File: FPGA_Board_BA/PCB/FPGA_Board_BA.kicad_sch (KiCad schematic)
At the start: 0 parts

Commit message: started component placement
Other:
- note added: "TODO: - 25uF Kondensator -> 3 mal 10uF [X] Extra 5VA für Tamura Sensoren [X] INA Spannungspegel / Bereich Prüfen [X] SMD 2*4 pin (2.54 pitch) stecker suchen Stiftleiste [X] Wannenstecker / Buchse für FPGA free Pins (26pin) kein 5VA, zweite Reihe Für GND - ESD Protection für Tamura PinHeaders - Silkscreen bei FPGA korrigieren - Matchy 3D model für Plug Terminals"
- note removed: "TODO: - 25uF Kondensator -> 3 mal 10uF [X] Extra 5VA für Tamura Sensoren [X] INA Spannungspegel / Bereich Prüfen [X] SMD 2*4 pin (2.54 pitch) stecker suchen Stiftleiste [X] Wannenstecker / Buchse für FPGA free Pins (26pin) kein 5VA, zweite Reihe Für GND"
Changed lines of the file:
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@@
 	(generator_version "9.0")
 	(paper "A3")
-	(text "TODO:\n- 25uF Kondensator -> 3 mal 10uF \n[X] Extra 5VA für Tamura Sensoren\n[X] INA Spannungspegel / Bereich Prüfen\n[X] SMD 2*4 pin (2.54 pitch) stecker suchen Stiftleiste\n[X] Wannenstecker / Buchse für FPGA free Pins (26pin) kein 5VA, zweite Reihe\nFür GND"
+	(text "TODO:\n- 25uF Kondensator -> 3 mal 10uF \n[X] Extra 5VA für Tamura Sensoren\n[X] INA Spannungspegel / Bereich Prüfen\n[X] SMD 2*4 pin (2.54 pitch) stecker suchen Stiftleiste\n[X] Wannenstecker / Buchse für FPGA free Pins (26pin) kein 5VA, zweite Reihe\nFür GND\n- ESD Protection für Tamura PinHeaders\n- Silkscreen bei FPGA korrigieren\n- Matchy 3D model für Plug Terminals"
 		(exclude_from_sim no)
 		(at 328.422 239.268 0)

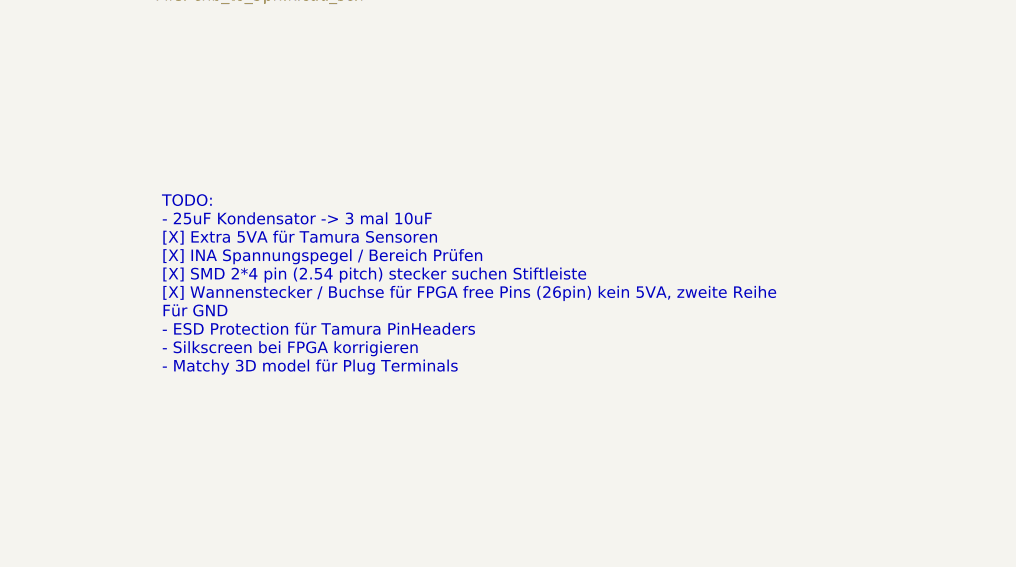
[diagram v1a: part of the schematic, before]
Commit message: arranged level shifters in schematic + solid progress in layout
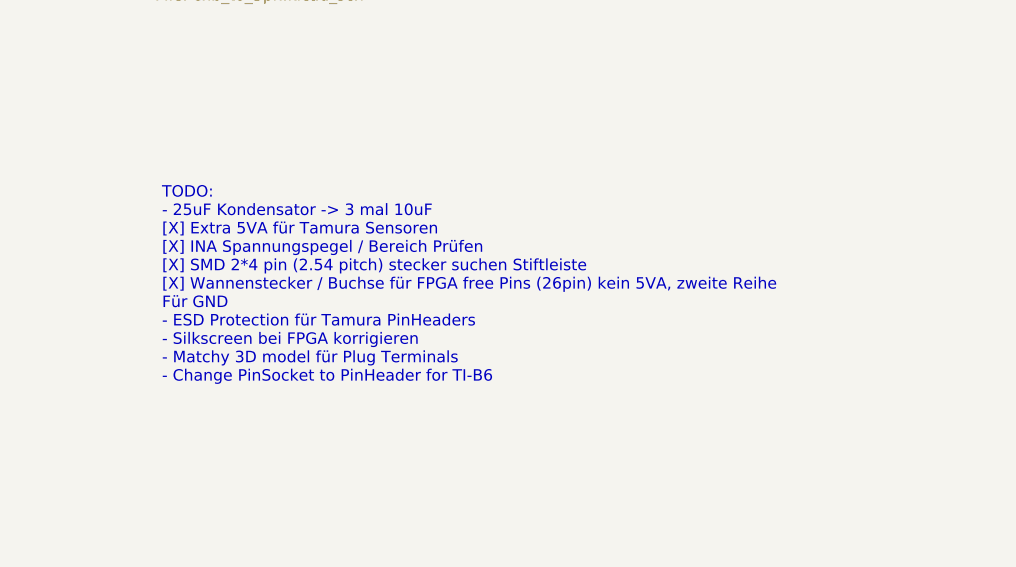
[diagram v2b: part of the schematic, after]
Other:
- note added: "TODO: - 25uF Kondensator -> 3 mal 10uF [X] Extra 5VA für Tamura Sensoren [X] INA Spannungspegel / Bereich Prüfen [X] SMD 2*4 pin (2.54 pitch) stecker suchen Stiftleiste [X] Wannenstecker / Buchse für FPGA free Pins (26pin) kein 5VA, zweite Reihe Für GND - ESD Protection für Tamura PinHeaders - Silkscreen bei FPGA korrigieren - Matchy 3D model für Plug Terminals - Change PinSocket to PinHeader for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"
- note removed: "TODO: - 25uF Kondensator -> 3 mal 10uF [X] Extra 5VA für Tamura Sensoren [X] INA Spannungspegel / Bereich Prüfen [X] SMD 2*4 pin (2.54 pitch) stecker suchen Stiftleiste [X] Wannenstecker / Buchse für FPGA free Pins (26pin) kein 5VA, zweite Reihe Für GND - ESD Protection für Tamura PinHeaders - Silkscreen bei FPGA korrigieren - Matchy 3D model für Plug Terminals"
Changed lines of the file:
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@@
 	(generator_version "9.0")
 	(paper "A3")
-	(text "TODO:\n- 25uF Kondensator -> 3 mal 10uF \n[X] Extra 5VA für Tamura Sensoren\n[X] INA Spannungspegel / Bereich Prüfen\n[X] SMD 2*4 pin (2.54 pitch) stecker suchen Stiftleiste\n[X] Wannenstecker / Buchse für FPGA free Pins (26pin) kein 5VA, zweite Reihe\nFür GND\n- ESD Protection für Tamura PinHeaders\n- Silkscreen bei FPGA korrigieren\n- Matchy 3D model für Plug Terminals"
+	(text "TODO:\n- 25uF Kondensator -> 3 mal 10uF \n[X] Extra 5VA für Tamura Sensoren\n[X] INA Spannungspegel / Bereich Prüfen\n[X] SMD 2*4 pin (2.54 pitch) stecker suchen Stiftleiste\n[X] Wannenstecker / Buchse für FPGA free Pins (26pin) kein 5VA, zweite Reihe\nFür GND\n- ESD Protection für Tamura PinHeaders\n- Silkscreen bei FPGA korrigieren\n- Matchy 3D model für Plug Terminals\n- Change PinSocket to PinHeader for TI-B6"
 		(exclude_from_sim no)
 		(at 328.422 239.268 0)

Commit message: layout of islands is ready
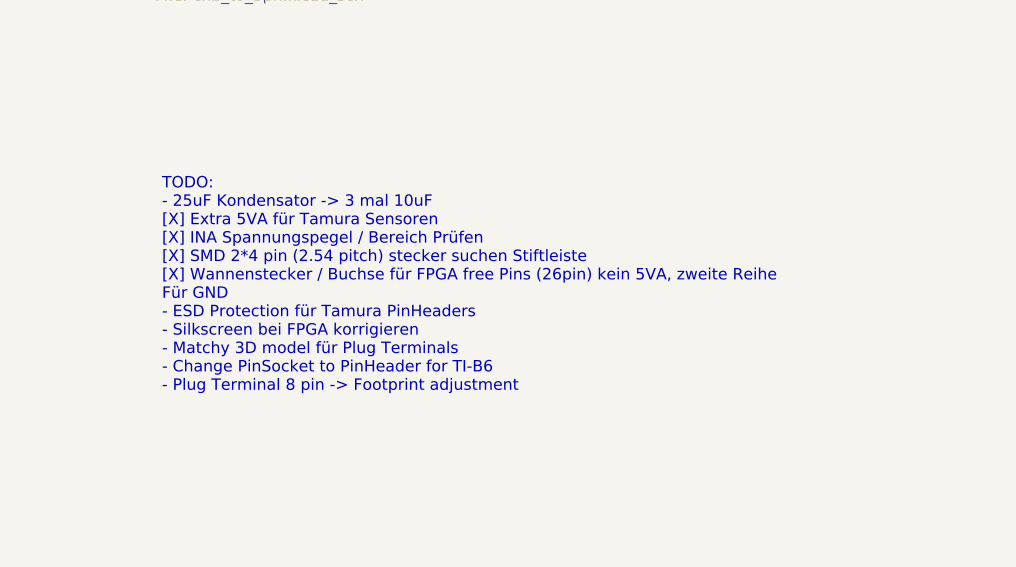
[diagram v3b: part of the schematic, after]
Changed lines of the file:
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@@
 	(generator_version "9.0")
 	(paper "A3")
-	(text "TODO:\n- 25uF Kondensator -> 3 mal 10uF \n[X] Extra 5VA für Tamura Sensoren\n[X] INA Spannungspegel / Bereich Prüfen\n[X] SMD 2*4 pin (2.54 pitch) stecker suchen Stiftleiste\n[X] Wannenstecker / Buchse für FPGA free Pins (26pin) kein 5VA, zweite Reihe\nFür GND\n- ESD Protection für Tamura PinHeaders\n- Silkscreen bei FPGA korrigieren\n- Matchy 3D model für Plug Terminals\n- Change PinSocket to PinHeader for TI-B6"
+	(text "TODO:\n- 25uF Kondensator -> 3 mal 10uF \n[X] Extra 5VA für Tamura Sensoren\n[X] INA Spannungspegel / Bereich Prüfen\n[X] SMD 2*4 pin (2.54 pitch) stecker suchen Stiftleiste\n[X] Wannenstecker / Buchse für FPGA free Pins (26pin) kein 5VA, zweite Reihe\nFür GND\n- ESD Protection für Tamura PinHeaders\n- Silkscreen bei FPGA korrigieren\n- Matchy 3D model für Plug Terminals\n- Change PinSocket to PinHeader for TI-B6\n- Plug Terminal 8 pin -> Footprint adjustment"
 		(exclude_from_sim no)
 		(at 328.422 239.268 0)

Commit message: Component placement ready. Waiting to meet with Leo
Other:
- note added: "TODO: - 25uF Kondensator -> 3 mal 10uF [X] Extra 5VA für Tamura Sensoren [X] INA Spannungspegel / Bereich Prüfen [X] SMD 2*4 pin (2.54 pitch) stecker suchen Stiftleiste [X] Wannenstecker / Buchse für FPGA free Pins (26pin) kein 5VA, zweite Reihe Für GND - ESD Protection für Tamura PinHeaders - Silkscreen bei FPGA korrigieren - Matchy 3D model für Plug Terminals - Change PinSocket to PinHeader (SM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"
- note removed: "TODO: - 25uF Kondensator -> 3 mal 10uF [X] Extra 5VA für Tamura Sensoren [X] INA Spannungspegel / Bereich Prüfen [X] SMD 2*4 pin (2.54 pitch) stecker suchen Stiftleiste [X] Wannenstecker / Buchse für FPGA free Pins (26pin) kein 5VA, zweite Reihe Für GND - ESD Protection für Tamura PinHeaders - Silkscreen bei FPGA korrigieren - Matchy 3D model für Plug Terminals - Change PinSocket to PinHeader for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"
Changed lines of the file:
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@@
 	(generator_version "9.0")
 	(paper "A3")
-	(text "TODO:\n- 25uF Kondensator -> 3 mal 10uF \n[X] Extra 5VA für Tamura Sensoren\n[X] INA Spannungspegel / Bereich Prüfen\n[X] SMD 2*4 pin (2.54 pitch) stecker suchen Stiftleiste\n[X] Wannenstecker / Buchse für FPGA free Pins (26pin) kein 5VA, zweite Reihe\nFür GND\n- ESD Protection für Tamura PinHeaders\n- Silkscreen bei FPGA korrigieren\n- Matchy 3D model für Plug Terminals\n- Change PinSocket to PinHeader for TI-B6\n- Plug Terminal 8 pin -> Footprint adjustment"
+	(text "TODO:\n- 25uF Kondensator -> 3 mal 10uF \n[X] Extra 5VA für Tamura Sensoren\n[X] INA Spannungspegel / Bereich Prüfen\n[X] SMD 2*4 pin (2.54 pitch) stecker suchen Stiftleiste\n[X] Wannenstecker / Buchse für FPGA free Pins (26pin) kein 5VA, zweite Reihe\nFür GND\n- ESD Protection für Tamura PinHeaders\n- Silkscreen bei FPGA korrigieren\n- Matchy 3D model für Plug Terminals\n- Change PinSocket to PinHeader (SMD) for TI-B6\n- Plug Terminal 8 pin -> Footprint adjustment\n[X] Fix Footprint of 5VA Inductor"
 		(exclude_from_sim no)
-		(at 328.422 239.268 0)
+		(at 327.66 232.156 0)
 		(effects
 			(font
